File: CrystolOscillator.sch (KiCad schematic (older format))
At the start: 4 parts, among them Y1 32.768kHz, Y2 48MHz

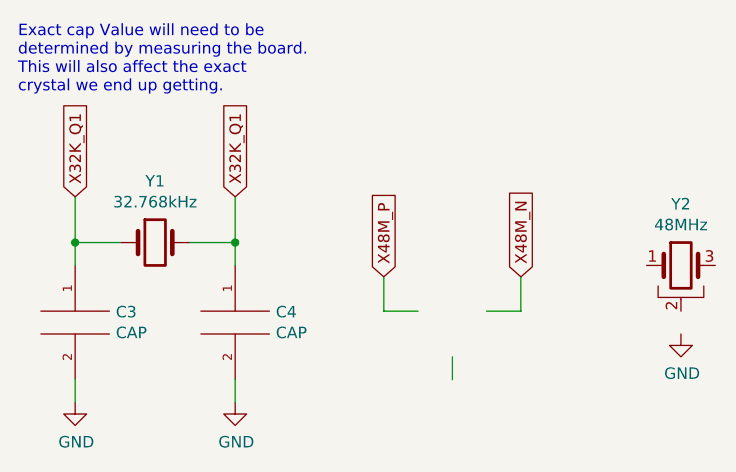
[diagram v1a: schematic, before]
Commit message: part way through getting new ICs and other components back on the PCB
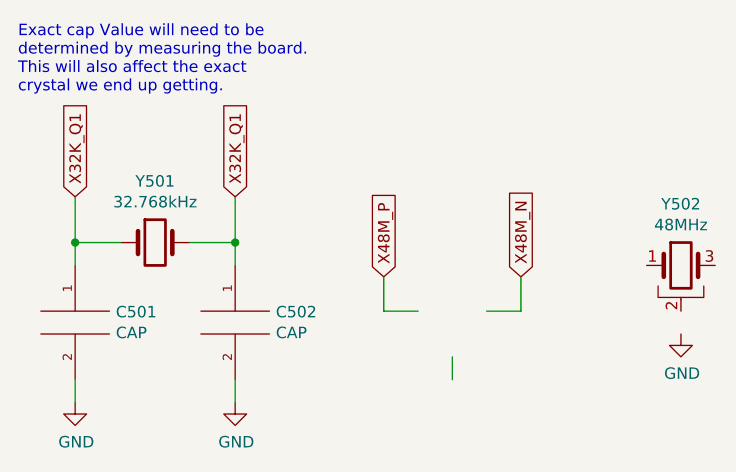
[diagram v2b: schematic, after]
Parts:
- renumbered C3 to C501, C4 to C502, Y1 to Y501, Y2 to Y502
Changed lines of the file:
@@
 $EndDescr
 $Comp
-L Device:Crystal Y1
+L Device:Crystal Y501
 U 1 1 613837BD
 P 2700 1750
-F 0 "Y1" H 2700 2018 50  0000 C CNN
+F 0 "Y501" H 2700 2018 50  0000 C CNN
 F 1 "32.768kHz" H 2700 1927 50  0000 C CNN
 F 2 "Crystal:Crystal_SMD_2012-2Pin_2.0x1.2mm_HandSoldering" H 2700 1750 50  0001 C CNN
@@
 $EndComp
 $Comp
-L Device:Crystal_GND2 Y2
+L Device:Crystal_GND2 Y502
 U 1 1 613841EB
 P 5000 1850
-F 0 "Y2" H 5000 2118 50  0000 C CNN
+F 0 "Y502" H 5000 2118 50  0000 C CNN
 F 1 "48MHz" H 5000 2027 50  0000 C CNN
 F 2 "Crystal:Crystal_SMD_2016-4Pin_2.0x1.6mm" H 5000 1850 50  0001 C CNN
@@
 $EndComp
 $Comp
-L pspice:CAP C3
+L pspice:CAP C501
 U 1 1 61384AA5
 P 2350 2100
-F 0 "C3" H 2528 2146 50  0000 L CNN
+F 0 "C501" H 2528 2146 50  0000 L CNN
 F 1 "CAP" H 2528 2055 50  0000 L CNN
 F 2 "Capacitor_SMD:C_0805_2012Metric_Pad1.18x1.45mm_HandSolder" H 2350 2100 50  0001 C CNN
@@
 $EndComp
 $Comp
-L pspice:CAP C4
+L pspice:CAP C502
 U 1 1 61384ECD
 P 3050 2100
-F 0 "C4" H 3228 2146 50  0000 L CNN
+F 0 "C502" H 3228 2146 50  0000 L CNN
 F 1 "CAP" H 3228 2055 50  0000 L CNN
 F 2 "Capacitor_SMD:C_0805_2012Metric_Pad1.18x1.45mm_HandSolder" H 3050 2100 50  0001 C CNN
@@
 	3050 1750 3050 1850
 $Comp
-L power:GND #PWR0115
+L power:GND #PWR0503
 U 1 1 613863D7
 P 5000 2150
-F 0 "#PWR0115" H 5000 1900 50  0001 C CNN
+F 0 "#PWR0503" H 5000 1900 50  0001 C CNN
 F 1 "GND" H 5005 1977 50  0000 C CNN
 F 2 "" H 5000 2150 50  0001 C CNN
@@
 $EndComp
 $Comp
-L power:GND #PWR0110
+L power:GND #PWR0502
 U 1 1 613869EE
 P 3050 2450
-F 0 "#PWR0110" H 3050 2200 50  0001 C CNN
+F 0 "#PWR0502" H 3050 2200 50  0001 C CNN
 F 1 "GND" H 3055 2277 50  0000 C CNN
 F 2 "" H 3050 2450 50  0001 C CNN
@@
 $EndComp
 $Comp
-L power:GND #PWR0111
+L power:GND #PWR0501
 U 1 1 61386BC1
 P 2350 2450
-F 0 "#PWR0111" H 2350 2200 50  0001 C CNN
+F 0 "#PWR0501" H 2350 2200 50  0001 C CNN
 F 1 "GND" H 2355 2277 50  0000 C CNN
 F 2 "" H 2350 2450 50  0001 C CNN

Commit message: Added UI buttons, LEDs, Decoupling caps, MCU connections, and other good stuff.
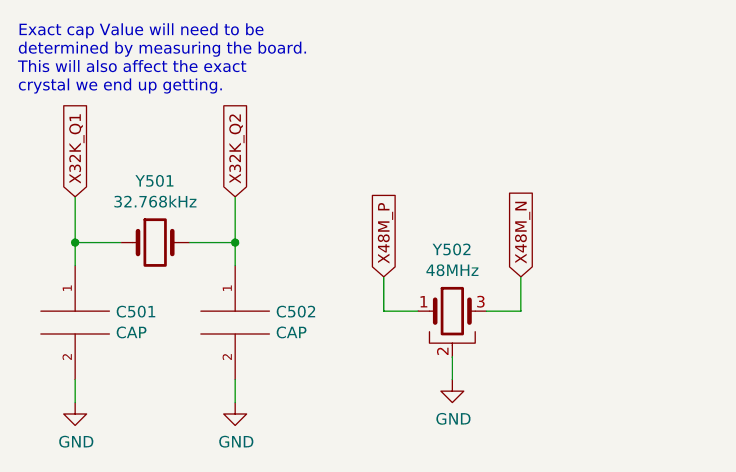
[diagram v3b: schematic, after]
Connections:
- net labels added: X32K_Q2
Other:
- moved on the sheet: Y502
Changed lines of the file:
@@
 $Descr A4 11693 8268
 encoding utf-8
-Sheet 5 5
+Sheet 5 6
 Title ""
 Date ""
@@
 L Device:Crystal_GND2 Y502
 U 1 1 613841EB
-P 5000 1850
-F 0 "Y502" H 5000 2118 50  0000 C CNN
-F 1 "48MHz" H 5000 2027 50  0000 C CNN
-F 2 "Crystal:Crystal_SMD_2016-4Pin_2.0x1.6mm" H 5000 1850 50  0001 C CNN
-F 3 "https://www.mouser.com/datasheet/2/909/cx2016db_e-1316650.pdf" H 5000 1850 50  0001 C CNN
-	1    5000 1850
+P 4000 2050
+F 0 "Y502" H 4000 2318 50  0000 C CNN
+F 1 "48MHz" H 4000 2227 50  0000 C CNN
+F 2 "Crystal:Crystal_SMD_2016-4Pin_2.0x1.6mm" H 4000 2050 50  0001 C CNN
+F 3 "https://www.mouser.com/datasheet/2/909/cx2016db_e-1316650.pdf" H 4000 2050 50  0001 C CNN
+	1    4000 2050
 	1    0    0    -1
 $EndComp
@@
 L power:GND #PWR0503
 U 1 1 613863D7
-P 5000 2150
-F 0 "#PWR0503" H 5000 1900 50  0001 C CNN
-F 1 "GND" H 5005 1977 50  0000 C CNN
-F 2 "" H 5000 2150 50  0001 C CNN
-F 3 "" H 5000 2150 50  0001 C CNN
-	1    5000 2150
+P 4000 2350
+F 0 "#PWR0503" H 4000 2100 50  0001 C CNN
+F 1 "GND" H 4005 2177 50  0000 C CNN
+F 2 "" H 4000 2350 50  0001 C CNN
+F 3 "" H 4000 2350 50  0001 C CNN
+	1    4000 2350
 	1    0    0    -1
 $EndComp
@@
 X32K_Q1
 Text GLabel 3050 1550 1    50   Input ~ 0
-X32K_Q1
+X32K_Q2
 Text Notes 2100 1100 0    50   ~ 0
 Exact cap Value will need to be \ndetermined by measuring the board. \nThis will also affect the exact \ncrystal we end up getting.
